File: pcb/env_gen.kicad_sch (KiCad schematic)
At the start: 20 parts, among them J9 AudioJack2, SW1 SW_Push, U4 TL074

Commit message: update vca
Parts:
- removed D3, D4: 1N4148, Diode_THT:D_DO-35_SOD27_P7.62mm_Horizontal, symbol Diode:1N4148
- added D1, D12: 1N4148, Diode_THT:D_DO-35_SOD27_P7.62mm_Horizontal, symbol Diode:1N4148
- C16, C17, C18, C5: footprint (none) -> Capacitor_THT:C_Disc_D6.0mm_W2.5mm_P5.00mm
- J9: footprint (none) -> Connector_Audio:Jack_3.5mm_CUI_SJ1-3513N_Horizontal
- R20, R21, R22, R23, R30, R31, R32, R33: footprint (none) -> Resistor_THT:R_Axial_DIN0207_L6.3mm_D2.5mm_P10.16mm_Horizontal
- RV3, RV4: footprint (none) -> Potentiometer_THT:Potentiometer_Bourns_PTV09A-1_Single_Vertical
- SW1: footprint (none) -> Button_Switch_Keyboard:SW_Cherry_MX_1.00u_PCB
- U4: footprint (none) -> Package_DIP:DIP-14_W7.62mm
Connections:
- net at U4.6 (-), U4.7: now also D1.1 (K), D12.2 (A)
- net at RV4.1: now also D1.2 (A)
- net at RV3.1: now also D12.1 (K)

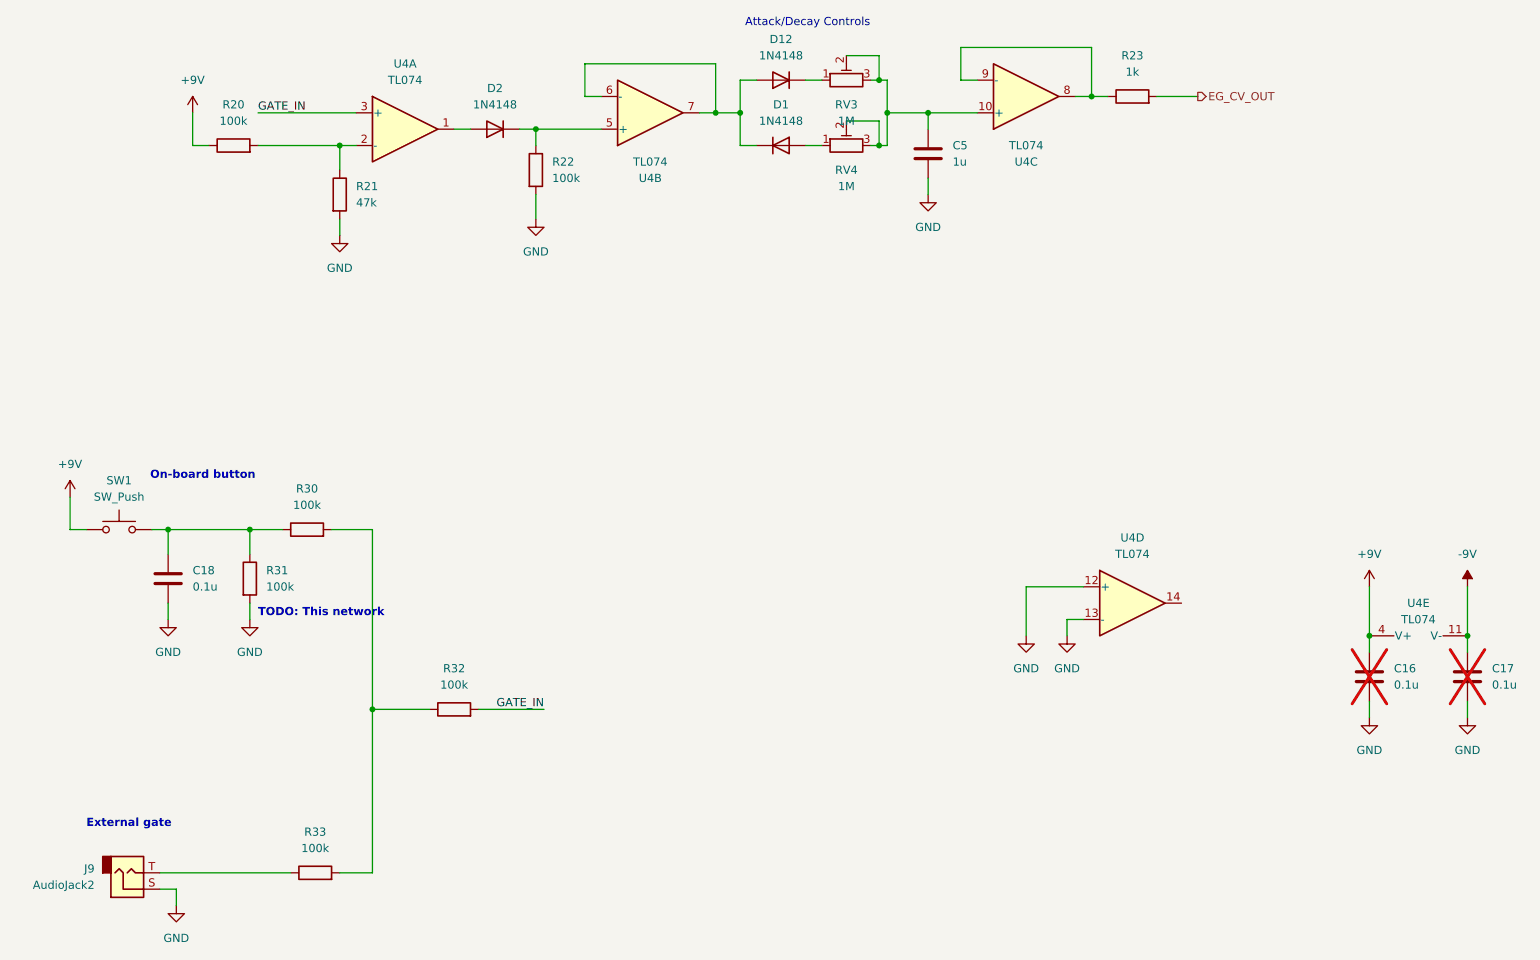
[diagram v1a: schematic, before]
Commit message: Fix some labeling and DNP statues
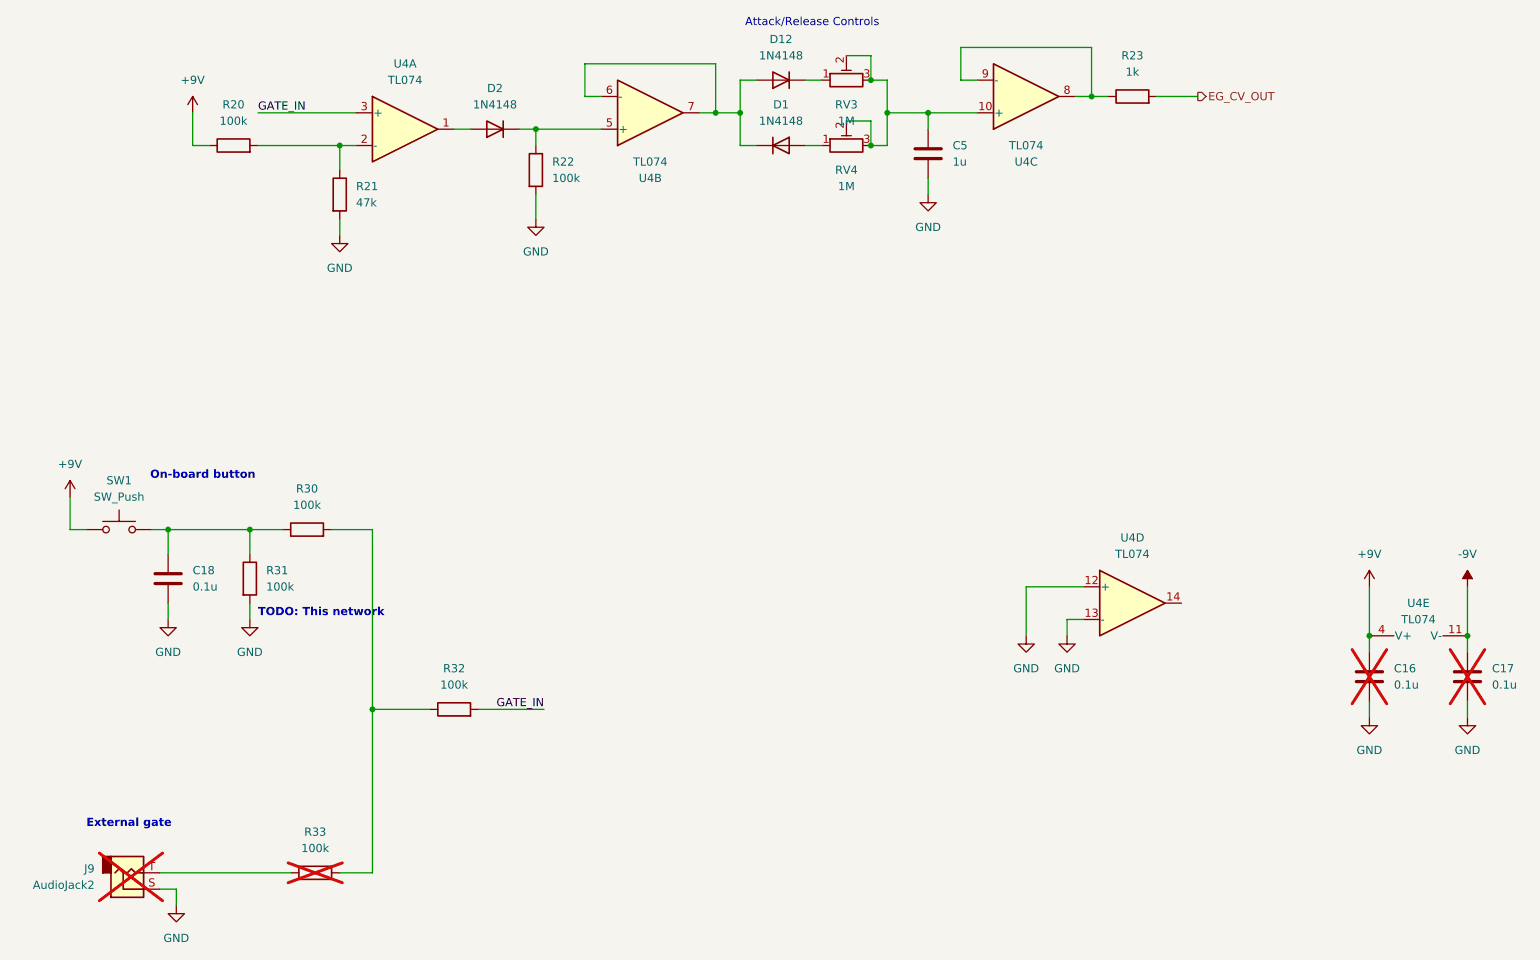
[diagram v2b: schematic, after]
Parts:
- J9, R33: now not fitted
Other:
- note added: "Attack/Release Controls"
- note removed: "Attack/Decay Controls"
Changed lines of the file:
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@@
 		)
 	)
-	(text "Attack/Decay Controls"
+	(text "Attack/Release Controls"
 		(exclude_from_sim no)
 		(at 153.162 49.53 0)
@@
 	)
 	(junction
-		(at 152.4 63.5)
+		(at 172.72 58.42)
 		(diameter 0)
 		(color 0 0 0 0)
 	)
 	(junction
-		(at 173.99 68.58)
+		(at 152.4 63.5)
 		(diameter 0)
 		(color 0 0 0 0)
@@
 	)
 	(junction
-		(at 265.43 144.78)
+		(at 172.72 68.58)
 		(diameter 0)
 		(color 0 0 0 0)
 	)
 	(junction
-		(at 173.99 58.42)
+		(at 265.43 144.78)
 		(diameter 0)
 		(color 0 0 0 0)
@@
 	(wire
 		(pts
-			(xy 173.99 68.58) (xy 172.72 68.58)
+			(xy 172.72 68.58) (xy 175.26 68.58)
 		)
 		(stroke
@@
 	(wire
 		(pts
-			(xy 173.99 64.77) (xy 173.99 68.58)
-		)
-		(stroke
-			(width 0)
-			(type default)
-		)
-	)
-	(wire
-		(pts
 			(xy 181.61 63.5) (xy 189.23 63.5)
 		)
@@
 	(wire
 		(pts
-			(xy 168.91 54.61) (xy 173.99 54.61)
-		)
-		(stroke
-			(width 0)
-			(type default)
-		)
-	)
-	(wire
-		(pts
 			(xy 95.25 128.27) (xy 95.25 156.21)
 		)
@@
 	(wire
 		(pts
-			(xy 168.91 64.77) (xy 173.99 64.77)
-		)
-		(stroke
-			(width 0)
-			(type default)
-		)
-	)
-	(wire
-		(pts
 			(xy 120.65 66.04) (xy 130.81 66.04)
 		)
@@
 	(wire
 		(pts
-			(xy 173.99 54.61) (xy 173.99 58.42)
+			(xy 175.26 58.42) (xy 175.26 63.5)
 		)
 		(stroke
@@
 	(wire
 		(pts
-			(xy 175.26 58.42) (xy 175.26 63.5)
+			(xy 181.61 66.04) (xy 181.61 63.5)
 		)
 		(stroke
@@
 	(wire
 		(pts
-			(xy 181.61 66.04) (xy 181.61 63.5)
+			(xy 60.96 128.27) (xy 63.5 128.27)
 		)
 		(stroke
@@
 	(wire
 		(pts
-			(xy 60.96 128.27) (xy 63.5 128.27)
+			(xy 63.5 128.27) (xy 76.2 128.27)
 		)
 		(stroke
@@
 	(wire
 		(pts
-			(xy 63.5 128.27) (xy 76.2 128.27)
+			(xy 189.23 58.42) (xy 186.69 58.42)
 		)
 		(stroke
@@
 	(wire
 		(pts
-			(xy 189.23 58.42) (xy 186.69 58.42)
+			(xy 172.72 58.42) (xy 175.26 58.42)
 		)
 		(stroke
@@
 	(wire
 		(pts
-			(xy 173.99 58.42) (xy 175.26 58.42)
+			(xy 95.25 181.61) (xy 95.25 156.21)
 		)
 		(stroke
@@
 	(wire
 		(pts
-			(xy 95.25 181.61) (xy 95.25 156.21)
+			(xy 148.59 55.88) (xy 148.59 63.5)
 		)
 		(stroke
@@
 	(wire
 		(pts
-			(xy 148.59 55.88) (xy 148.59 63.5)
+			(xy 172.72 54.61) (xy 172.72 58.42)
 		)
 		(stroke
@@
 	(wire
 		(pts
-			(xy 175.26 68.58) (xy 173.99 68.58)
+			(xy 172.72 64.77) (xy 172.72 68.58)
 		)
 		(stroke
@@
 	(wire
 		(pts
+			(xy 168.91 54.61) (xy 172.72 54.61)
+		)
+		(stroke
+			(width 0)
+			(type default)
+		)
+	)
+	(wire
+		(pts
 			(xy 207.01 53.34) (xy 207.01 60.96)
 		)
@@
 	(wire
 		(pts
-			(xy 172.72 58.42) (xy 173.99 58.42)
+			(xy 168.91 64.77) (xy 172.72 64.77)
 		)
 		(stroke
@@
 		(in_bom yes)
 		(on_board yes)
-		(dnp no)
+		(dnp yes)
 		(fields_autoplaced yes)
 		(property "Reference" "J9"
@@
 		(in_bom yes)
 		(on_board yes)
-		(dnp no)
+		(dnp yes)
 		(fields_autoplaced yes)
 		(property "Reference" "R33"
